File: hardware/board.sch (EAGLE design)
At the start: 45 parts, among them IC1 0915BM15A0001, J1 U.FL, U3 BLE113-A, X1 24MHz 8pF 10ppm -20C +70C, X3 MINI-USB-UX60-MB-5ST

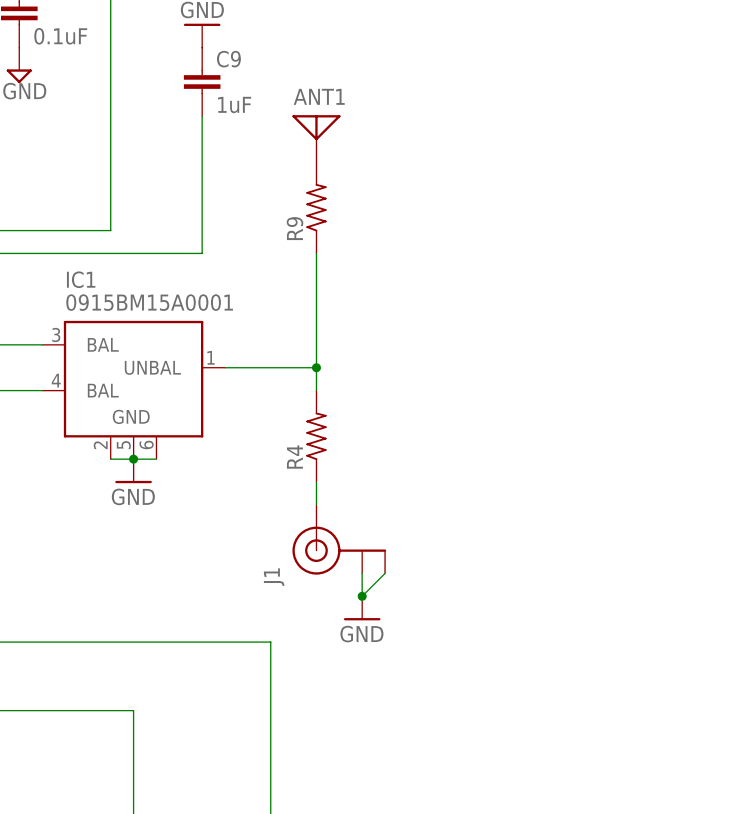
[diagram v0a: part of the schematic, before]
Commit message: Experiment: fix antenna test point
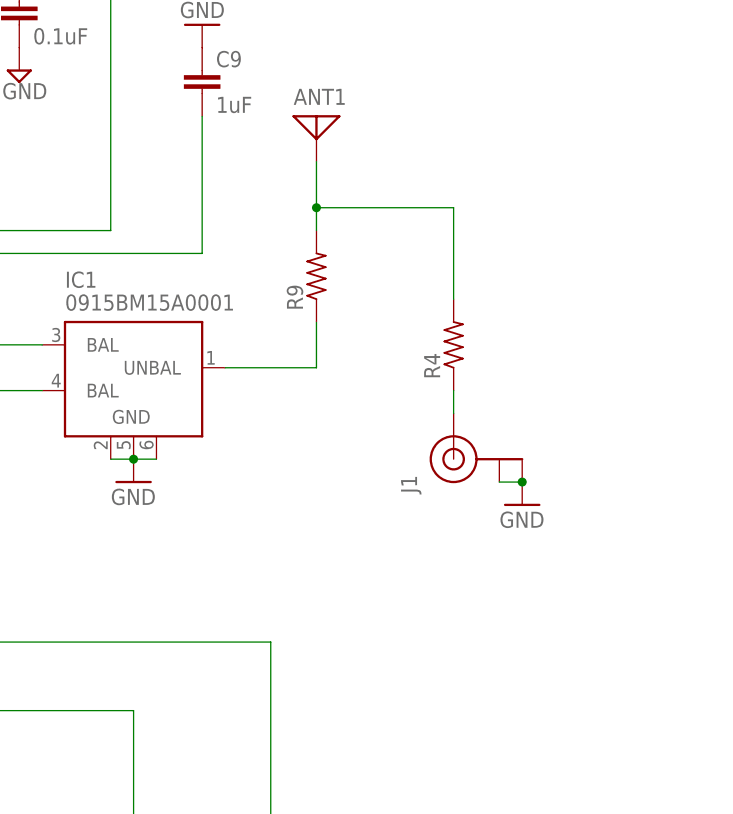
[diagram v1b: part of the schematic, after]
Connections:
- net N$10: no longer R4.2
- net N$12: now also R4.2
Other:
- moved on the sheet: J1, R4, R9
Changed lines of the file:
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@@
 <instance part="P+2" gate="1" x="-5.08" y="175.26"/>
 <instance part="SUPPLY5" gate="GND" x="76.2" y="-2.54"/>
-<instance part="J1" gate="G$1" x="152.4" y="35.56" rot="R90"/>
+<instance part="J1" gate="G$1" x="167.64" y="45.72" rot="R90"/>
 <instance part="U3" gate="G$1" x="60.96" y="-48.26" rot="MR180"/>
 <instance part="C5" gate="G$1" x="147.32" y="-17.78"/>
@@
 <instance part="IC1" gate="G$1" x="132.08" y="53.34"/>
 <instance part="GND10" gate="1" x="132.08" y="43.18"/>
-<instance part="R4" gate="G$1" x="152.4" y="48.26" rot="R90"/>
+<instance part="R4" gate="G$1" x="167.64" y="58.42" rot="R90"/>
 <instance part="ANT1" gate="A" x="152.4" y="83.82"/>
-<instance part="R9" gate="G$1" x="152.4" y="73.66" rot="R90"/>
+<instance part="R9" gate="G$1" x="152.4" y="66.04" rot="R90"/>
 <instance part="CC1110-DEBUG" gate="G$1" x="-17.78" y="55.88" rot="R180"/>
 <instance part="BLE113-DEBUG" gate="G$1" x="-15.24" y="-15.24" rot="R180"/>
@@
 <instance part="SUPPLY15" gate="GND" x="66.04" y="93.98"/>
 <instance part="SUPPLY18" gate="G$1" x="22.86" y="-68.58" rot="R180"/>
-<instance part="GND20" gate="1" x="157.48" y="27.94"/>
+<instance part="GND20" gate="1" x="175.26" y="40.64"/>
 <instance part="FID1" gate="G$1" x="111.76" y="-50.8"/>
 <instance part="FID2" gate="G$1" x="132.08" y="-50.8"/>
@@
 <pinref part="J1" gate="G$1" pin="GND@0"/>
 <pinref part="J1" gate="G$1" pin="GND@1"/>
-<wire x1="157.48" y1="30.48" x2="160.02" y2="33.02" width="0.1524" layer="91"/>
 <pinref part="GND20" gate="1" pin="GND"/>
-<junction x="157.48" y="30.48"/>
-<wire x1="157.48" y1="30.48" x2="157.48" y2="33.02" width="0.1524" layer="91"/>
+<junction x="175.26" y="43.18"/>
+<wire x1="175.26" y1="43.18" x2="172.72" y2="43.18" width="0.1524" layer="91"/>
 </segment>
 </net>
@@
 <pinref part="J1" gate="G$1" pin="SIGNAL"/>
 <pinref part="R4" gate="G$1" pin="1"/>
-<wire x1="152.4" y1="43.18" x2="152.4" y2="40.64" width="0.1524" layer="91"/>
+<wire x1="167.64" y1="53.34" x2="167.64" y2="50.8" width="0.1524" layer="91"/>
 </segment>
 </net>
 <net name="N$10" class="0">
 <segment>
-<pinref part="R4" gate="G$1" pin="2"/>
-<wire x1="152.4" y1="53.34" x2="152.4" y2="55.88" width="0.1524" layer="91"/>
 <pinref part="IC1" gate="G$1" pin="UNBAL"/>
 <wire x1="142.24" y1="55.88" x2="152.4" y2="55.88" width="0.1524" layer="91"/>
-<junction x="152.4" y="55.88"/>
 <pinref part="R9" gate="G$1" pin="1"/>
-<wire x1="152.4" y1="55.88" x2="152.4" y2="68.58" width="0.1524" layer="91"/>
+<wire x1="152.4" y1="55.88" x2="152.4" y2="60.96" width="0.1524" layer="91"/>
 </segment>
 </net>
@@
 <pinref part="ANT1" gate="A" pin="1"/>
 <pinref part="R9" gate="G$1" pin="2"/>
-</segment>
-</net>
+<wire x1="152.4" y1="71.12" x2="152.4" y2="73.66" width="0.1524" layer="91"/>
+<pinref part="R4" gate="G$1" pin="2"/>
+<wire x1="152.4" y1="73.66" x2="152.4" y2="78.74" width="0.1524" layer="91"/>
+<wire x1="167.64" y1="63.5" x2="167.64" y2="73.66" width="0.1524" layer="91"/>
+<wire x1="167.64" y1="73.66" x2="152.4" y2="73.66" width="0.1524" layer="91"/>
+<junction x="152.4" y="73.66"/>
+</segment>
+</net>
